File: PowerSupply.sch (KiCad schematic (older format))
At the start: 0 parts

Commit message: Arranged and annoted schematic
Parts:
- added C1, C2: CP, symbol Device:CP
- added D1, D2, D3, D4: 1N4007, Diode_THT:D_DO-41_SOD81_P10.16mm_Horizontal, symbol Diode:1N4007
- added D5, D6: LED, symbol Device:LED
- added J1: Barrel_Jack_Switch, symbol Connector:Barrel_Jack_Switch
- added J2, J3: Conn_02x02_Odd_Even, symbol Connector_Generic:Conn_02x02_Odd_Even
- added R1, R2: R, symbol Device:R
- added SW1: SW_DPDT_x2, symbol Switch:SW_DPDT_x2
- added U1: LM7805_TO220, Package_TO_SOT_THT:TO-220-3_Vertical, symbol Regulator_Linear:LM7805_TO220
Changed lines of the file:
@@
 Comment4 ""
 $EndDescr
+$Comp
+L Regulator_Linear:LM7805_TO220 U1
+U 1 1 5CD35ECB
+P 6625 3800
+F 0 "U1" H 6625 4042 50  0000 C CNN
+F 1 "LM7805_TO220" H 6625 3951 50  0000 C CNN
+F 2 "Package_TO_SOT_THT:TO-220-3_Vertical" H 6625 4025 50  0001 C CIN
+F 3 "http://www.fairchildsemi.com/ds/LM/LM7805.pdf" H 6625 3750 50  0001 C CNN
+	1    6625 3800
+	1    0    0    -1
+$EndComp
+$Comp
+L Diode:1N4007 D1
+U 1 1 5CD37B26
+P 4425 3950
+F 0 "D1" V 4379 4029 50  0000 L CNN
+F 1 "1N4007" V 4470 4029 50  0000 L CNN
+F 2 "Diode_THT:D_DO-41_SOD81_P10.16mm_Horizontal" H 4425 3775 50  0001 C CNN
+F 3 "http://www.vishay.com/docs/88503/1n4001.pdf" H 4425 3950 50  0001 C CNN
+	1    4425 3950
+	0    1    1    0
+$EndComp
+$Comp
+L Diode:1N4007 D3
+U 1 1 5CD3F3AA
+P 5075 3950
+F 0 "D3" V 5029 4029 50  0000 L CNN
+F 1 "1N4007" V 5120 4029 50  0000 L CNN
+F 2 "Diode_THT:D_DO-41_SOD81_P10.16mm_Horizontal" H 5075 3775 50  0001 C CNN
+F 3 "http://www.vishay.com/docs/88503/1n4001.pdf" H 5075 3950 50  0001 C CNN
+	1    5075 3950
+	0    1    1    0
+$EndComp
+$Comp
+L Diode:1N4007 D2
+U 1 1 5CD3FE81
+P 4425 4550
+F 0 "D2" V 4379 4629 50  0000 L CNN
+F 1 "1N4007" V 4470 4629 50  0000 L CNN
+F 2 "Diode_THT:D_DO-41_SOD81_P10.16mm_Horizontal" H 4425 4375 50  0001 C CNN
+F 3 "http://www.vishay.com/docs/88503/1n4001.pdf" H 4425 4550 50  0001 C CNN
+	1    4425 4550
+	0    1    1    0
+$EndComp
+$Comp
+L Diode:1N4007 D4
+U 1 1 5CD40742
+P 5075 4550
+F 0 "D4" V 5029 4629 50  0000 L CNN
+F 1 "1N4007" V 5120 4629 50  0000 L CNN
+F 2 "Diode_THT:D_DO-41_SOD81_P10.16mm_Horizontal" H 5075 4375 50  0001 C CNN
+F 3 "http://www.vishay.com/docs/88503/1n4001.pdf" H 5075 4550 50  0001 C CNN
+	1    5075 4550
+	0    1    1    0
+$EndComp
+$Comp
+L Device:CP C1
+U 1 1 5CD41669
+P 5825 3925
+F 0 "C1" H 5943 3971 50  0000 L CNN
+F 1 "CP" H 5943 3880 50  0000 L CNN
+F 2 "" H 5863 3775 50  0001 C CNN
+F 3 "~" H 5825 3925 50  0001 C CNN
+	1    5825 3925
+	1    0    0    -1
+$EndComp
+$Comp
+L Device:CP C2
+U 1 1 5CD42457
+P 7300 3925
+F 0 "C2" H 7418 3971 50  0000 L CNN
+F 1 "CP" H 7418 3880 50  0000 L CNN
+F 2 "" H 7338 3775 50  0001 C CNN
+F 3 "~" H 7300 3925 50  0001 C CNN
+	1    7300 3925
+	1    0    0    -1
+$EndComp
+$Comp
+L Device:LED D6
+U 1 1 5CD42B2D
+P 8925 4400
+F 0 "D6" V 8964 4283 50  0000 R CNN
+F 1 "LED" V 8873 4283 50  0000 R CNN
+F 2 "" H 8925 4400 50  0001 C CNN
+F 3 "~" H 8925 4400 50  0001 C CNN
+	1    8925 4400
+	0    -1   -1   0
+$EndComp
+$Comp
+L Device:LED D5
+U 1 1 5CD441AD
+P 7825 4400
+F 0 "D5" V 7864 4283 50  0000 R CNN
+F 1 "LED" V 7773 4283 50  0000 R CNN
+F 2 "" H 7825 4400 50  0001 C CNN
+F 3 "~" H 7825 4400 50  0001 C CNN
+	1    7825 4400
+	0    -1   -1   0
+$EndComp
+$Comp
+L Device:R R1
+U 1 1 5CD44A91
+P 7825 3900
+F 0 "R1" H 7755 3854 50  0000 R CNN
+F 1 "R" H 7755 3945 50  0000 R CNN
+F 2 "" V 7755 3900 50  0001 C CNN
+F 3 "~" H 7825 3900 50  0001 C CNN
+	1    7825 3900
+	-1   0    0    1
+$EndComp
+$Comp
+L Device:R R2
+U 1 1 5CD45C68
+P 8925 3900
+F 0 "R2" H 8855 3854 50  0000 R CNN
+F 1 "R" H 8855 3945 50  0000 R CNN
+F 2 "" V 8855 3900 50  0001 C CNN
+F 3 "~" H 8925 3900 50  0001 C CNN
+	1    8925 3900
+	-1   0    0    1
+$EndComp
+$Comp
+L Switch:SW_DPDT_x2 SW1
+U 1 1 5CD465F3
+P 8425 4175
+F 0 "SW1" H 8425 4460 50  0000 C CNN
+F 1 "SW_DPDT_x2" H 8425 4369 50  0000 C CNN
+F 2 "" H 8425 4175 50  0001 C CNN
+F 3 "~" H 8425 4175 50  0001 C CNN
+	1    8425 4175
+	1    0    0    -1
+$EndComp
+$Comp
+L Connector_Generic:Conn_02x02_Odd_Even J2
+U 1 1 5CD47BF0
+P 9800 3925
+F 0 "J2" H 9850 4142 50  0000 C CNN
+F 1 "Conn_02x02_Odd_Even" H 9850 4051 50  0000 C CNN
+F 2 "" H 9800 3925 50  0001 C CNN
+F 3 "~" H 9800 3925 50  0001 C CNN
+	1    9800 3925
+	1    0    0    -1
+$EndComp
+$Comp
+L Connector_Generic:Conn_02x02_Odd_Even J3
+U 1 1 5CD48B93
+P 9800 4475
+F 0 "J3" H 9850 4692 50  0000 C CNN
+F 1 "Conn_02x02_Odd_Even" H 9850 4601 50  0000 C CNN
+F 2 "" H 9800 4475 50  0001 C CNN
+F 3 "~" H 9800 4475 50  0001 C CNN
+	1    9800 4475
+	1    0    0    -1
+$EndComp
+$Comp
+L Connector:Barrel_Jack_Switch J1
+U 1 1 5CD495E1
+P 3825 4325
+F 0 "J1" H 3882 4642 50  0000 C CNN
+F 1 "Barrel_Jack_Switch" H 3882 4551 50  0000 C CNN
+F 2 "" H 3875 4285 50  0001 C CNN
+F 3 "~" H 3875 4285 50  0001 C CNN
+	1    3825 4325
+	1    0    0    -1
+$EndComp
 $EndSCHEMATC

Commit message: Added footprint associations to schematic components
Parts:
- C1: footprint (none) -> Capacitor_THT:CP_Radial_D10.0mm_P5.00mm
- C2: footprint (none) -> Capacitor_THT:CP_Radial_D6.3mm_P2.50mm
- D5, D6: footprint (none) -> LED_THT:LED_D5.0mm
- J1: footprint (none) -> Connector_BarrelJack:BarrelJack_CUI_PJ-102AH_Horizontal
- J2, J3: footprint (none) -> Connector_PinHeader_2.54mm:PinHeader_2x02_P2.54mm_Vertical
- R1, R2: footprint (none) -> Resistor_THT:R_Axial_DIN0207_L6.3mm_D2.5mm_P7.62mm_Horizontal
- SW1: footprint (none) -> digikey-footprints:Switch_Slide_11.6x4mm_EG1218
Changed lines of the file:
@@
 F 0 "C1" H 5943 3971 50  0000 L CNN
 F 1 "CP" H 5943 3880 50  0000 L CNN
-F 2 "" H 5863 3775 50  0001 C CNN
+F 2 "Capacitor_THT:CP_Radial_D10.0mm_P5.00mm" H 5863 3775 50  0001 C CNN
 F 3 "~" H 5825 3925 50  0001 C CNN
 	1    5825 3925
@@
 F 0 "C2" H 7418 3971 50  0000 L CNN
 F 1 "CP" H 7418 3880 50  0000 L CNN
-F 2 "" H 7338 3775 50  0001 C CNN
+F 2 "Capacitor_THT:CP_Radial_D6.3mm_P2.50mm" H 7338 3775 50  0001 C CNN
 F 3 "~" H 7300 3925 50  0001 C CNN
 	1    7300 3925
@@
 F 0 "D6" V 8964 4283 50  0000 R CNN
 F 1 "LED" V 8873 4283 50  0000 R CNN
-F 2 "" H 8925 4400 50  0001 C CNN
+F 2 "LED_THT:LED_D5.0mm" H 8925 4400 50  0001 C CNN
 F 3 "~" H 8925 4400 50  0001 C CNN
 	1    8925 4400
@@
 F 0 "D5" V 7864 4283 50  0000 R CNN
 F 1 "LED" V 7773 4283 50  0000 R CNN
-F 2 "" H 7825 4400 50  0001 C CNN
+F 2 "LED_THT:LED_D5.0mm" H 7825 4400 50  0001 C CNN
 F 3 "~" H 7825 4400 50  0001 C CNN
 	1    7825 4400
@@
 F 0 "R1" H 7755 3854 50  0000 R CNN
 F 1 "R" H 7755 3945 50  0000 R CNN
-F 2 "" V 7755 3900 50  0001 C CNN
+F 2 "Resistor_THT:R_Axial_DIN0207_L6.3mm_D2.5mm_P7.62mm_Horizontal" V 7755 3900 50  0001 C CNN
 F 3 "~" H 7825 3900 50  0001 C CNN
 	1    7825 3900
@@
 F 0 "R2" H 8855 3854 50  0000 R CNN
 F 1 "R" H 8855 3945 50  0000 R CNN
-F 2 "" V 8855 3900 50  0001 C CNN
+F 2 "Resistor_THT:R_Axial_DIN0207_L6.3mm_D2.5mm_P7.62mm_Horizontal" V 8855 3900 50  0001 C CNN
 F 3 "~" H 8925 3900 50  0001 C CNN
 	1    8925 3900
@@
 F 0 "SW1" H 8425 4460 50  0000 C CNN
 F 1 "SW_DPDT_x2" H 8425 4369 50  0000 C CNN
-F 2 "" H 8425 4175 50  0001 C CNN
+F 2 "digikey-footprints:Switch_Slide_11.6x4mm_EG1218" H 8425 4175 50  0001 C CNN
 F 3 "~" H 8425 4175 50  0001 C CNN
 	1    8425 4175
@@
 F 0 "J2" H 9850 4142 50  0000 C CNN
 F 1 "Conn_02x02_Odd_Even" H 9850 4051 50  0000 C CNN
-F 2 "" H 9800 3925 50  0001 C CNN
+F 2 "Connector_PinHeader_2.54mm:PinHeader_2x02_P2.54mm_Vertical" H 9800 3925 50  0001 C CNN
 F 3 "~" H 9800 3925 50  0001 C CNN
 	1    9800 3925
@@
 F 0 "J3" H 9850 4692 50  0000 C CNN
 F 1 "Conn_02x02_Odd_Even" H 9850 4601 50  0000 C CNN
-F 2 "" H 9800 4475 50  0001 C CNN
+F 2 "Connector_PinHeader_2.54mm:PinHeader_2x02_P2.54mm_Vertical" H 9800 4475 50  0001 C CNN
 F 3 "~" H 9800 4475 50  0001 C CNN
 	1    9800 4475
@@
 F 0 "J1" H 3882 4642 50  0000 C CNN
 F 1 "Barrel_Jack_Switch" H 3882 4551 50  0000 C CNN
-F 2 "" H 3875 4285 50  0001 C CNN
+F 2 "Connector_BarrelJack:BarrelJack_CUI_PJ-102AH_Horizontal" H 3875 4285 50  0001 C CNN
 F 3 "~" H 3875 4285 50  0001 C CNN
 	1    3825 4325

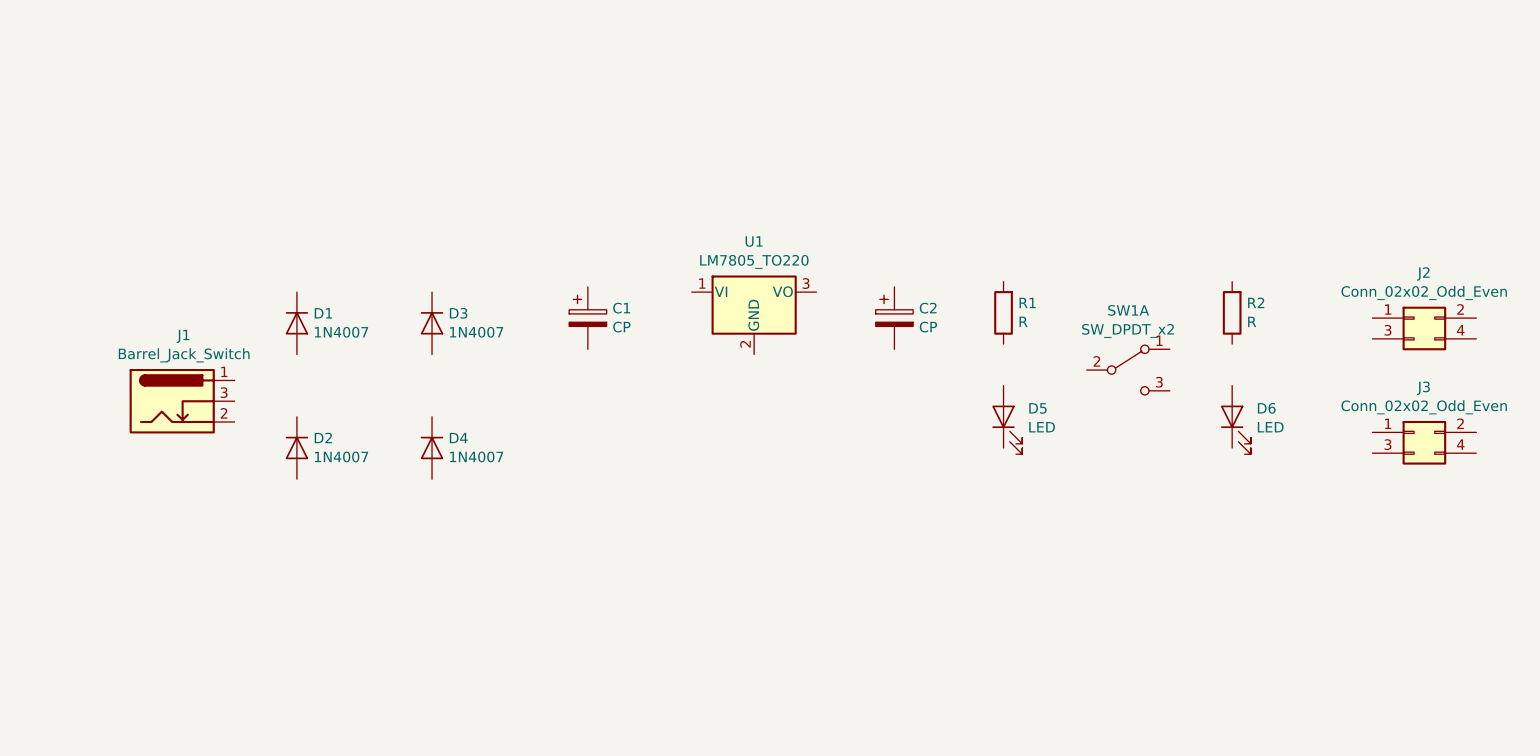
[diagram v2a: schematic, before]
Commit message: Completed the wiring of the schematic
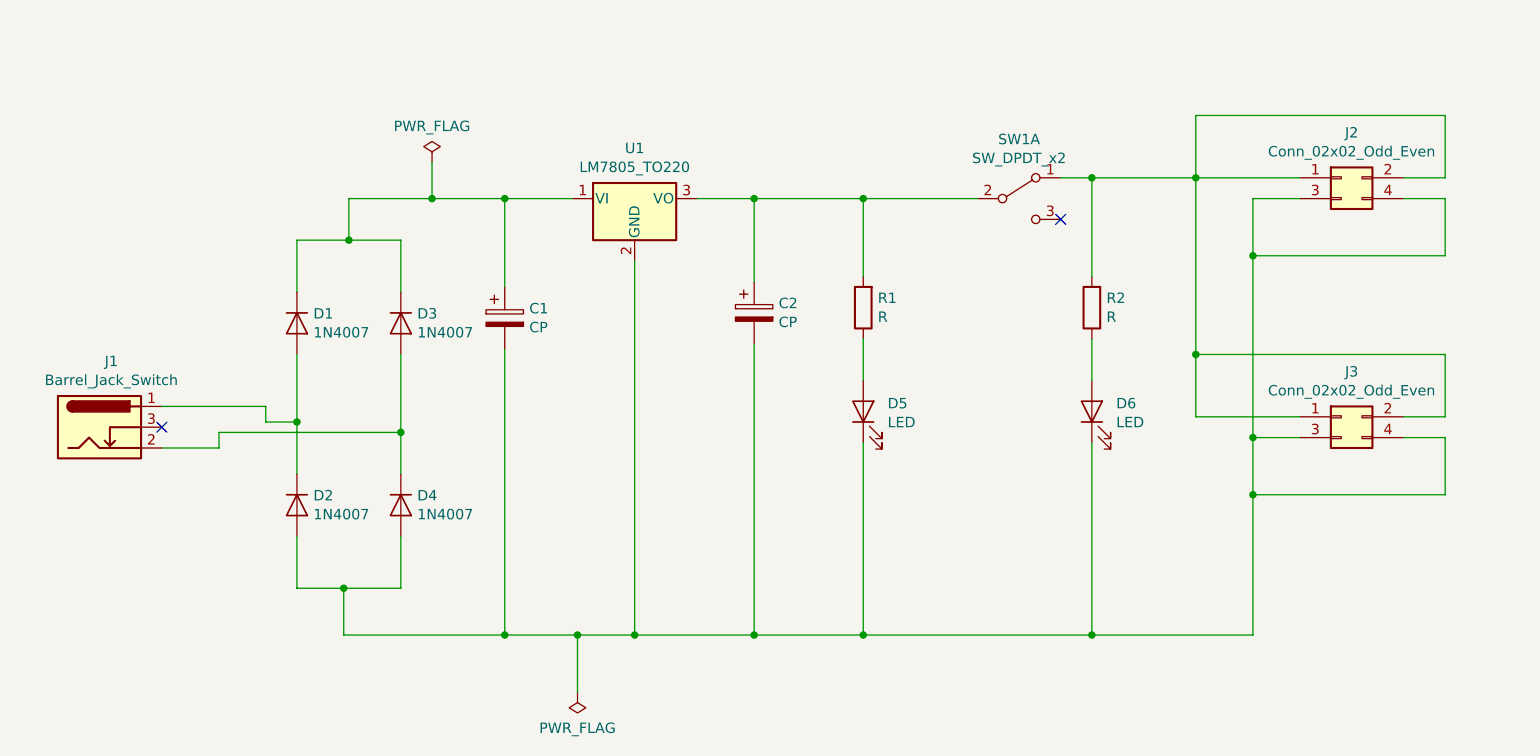
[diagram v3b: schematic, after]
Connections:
- net at U1.1 (VI): now also C1.1, D1.1 (K), D3.1 (K)
- net at U1.2 (GND): now also C1.2, C2.2, D2.2 (A), D4.2 (A), D5.1 (K), D6.1 (K), J2.3 (Pin_3), J2.4 (Pin_4), J3.3 (Pin_3), J3.4 (Pin_4)
- net at U1.3 (VO): now also C2.1, R1.2, SW1.2 (B)
- net at D1.2 (A): now also D2.1 (K), J1.1
- net at D3.2 (A): now also D4.1 (K), J1.2
- net at D6.2 (A): now also R2.1
- net at D5.2 (A): now also R1.1
- net at R2.2: now also J2.1 (Pin_1), J2.2 (Pin_2), J3.1 (Pin_1), J3.2 (Pin_2), SW1.1 (A)
- no-connect marks 0 -> 2
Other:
- moved on the sheet: C1, C2, D2, D3, D4, D5, D6, J1, J2, J3, R1, R2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

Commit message: Added Nets to schematic
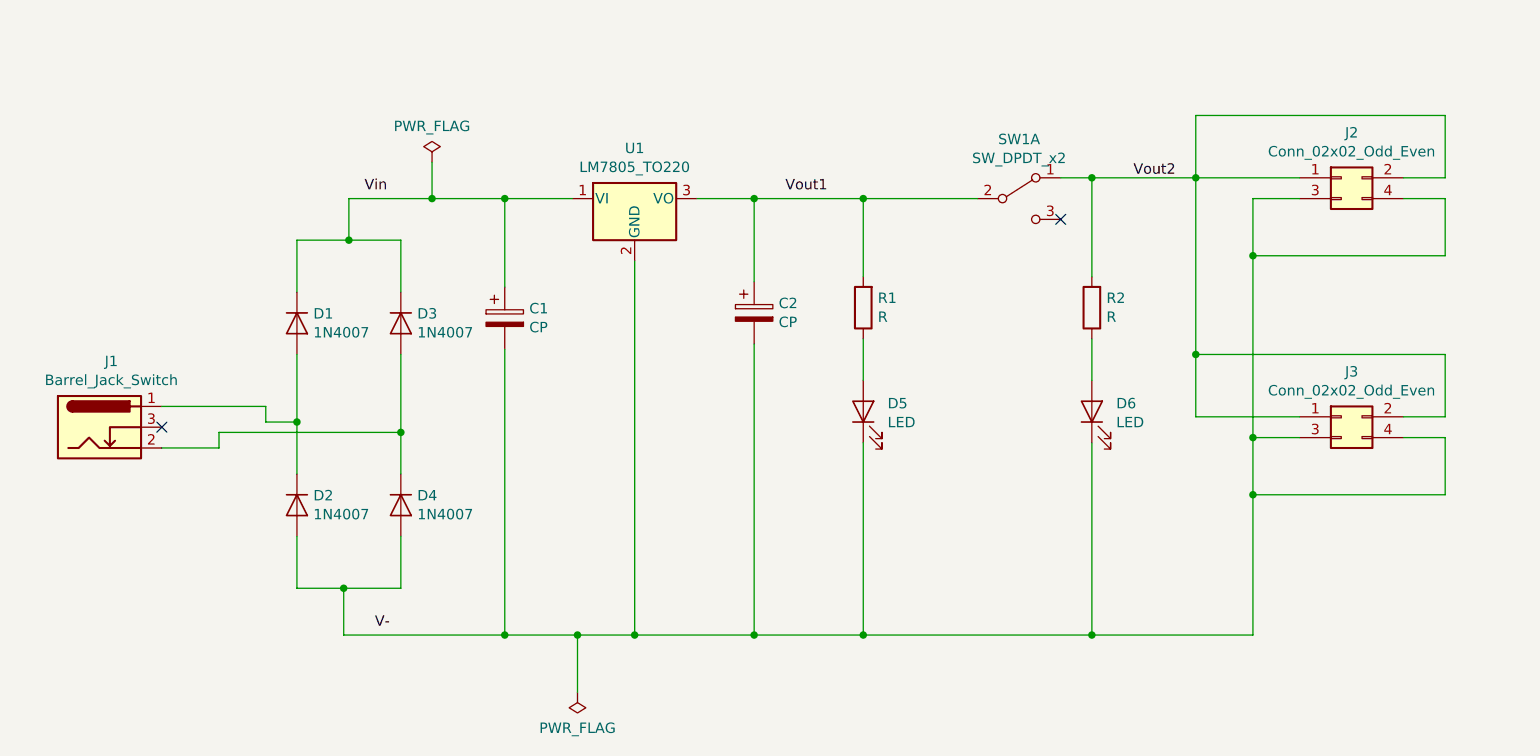
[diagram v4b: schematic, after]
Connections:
- net Vout2: now reaches J2.1 (Pin_1), J2.2 (Pin_2), J3.1 (Pin_1), J3.2 (Pin_2), R2.2, SW1.1 (A)
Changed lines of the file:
@@
 Wire Wire Line
 	5775 5450 6050 5450
+Text Label 4750 3325 0    50   ~ 0
+Vin
+Text Label 4800 5425 0    50   ~ 0
+V-
+Text Label 6775 3325 0    50   ~ 0
+Vout1
+Text Label 8450 3250 0    50   ~ 0
+Vout2
 $EndSCHEMATC

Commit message: Added comment notes
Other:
- note added: "N1 - Power Input"
- note added: "N2 - Bridge Rectifier"
- note added: "N3 - Voltage Regulator"
- note added: "N4 -\nPower\nIndicator"
- note added: "N5 - \nOn/Off Switch"
- note added: "N6 - \nOutput\nPWR Indicator"
- note added: "N7 - Power Output"
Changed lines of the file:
@@
 Text Label 8450 3250 0    50   ~ 0
 Vout2
+Wire Notes Line
+	4025 2750 4025 5750
+Wire Notes Line
+	4025 5750 3075 5750
+Wire Notes Line
+	3075 5750 3075 2750
+Wire Notes Line
+	3075 2750 4025 2750
+Wire Notes Line
+	4225 2750 4225 5750
+Wire Notes Line
+	4225 5750 5250 5750
+Wire Notes Line
+	5250 5750 5250 2750
+Wire Notes Line
+	5250 2750 4225 2750
+Wire Notes Line
+	5325 2750 5325 5750
+Wire Notes Line
+	5325 5750 7000 5750
+Wire Notes Line
+	7000 5750 7000 2750
+Wire Notes Line
+	7000 2750 5325 2750
+Wire Notes Line
+	7075 2750 7075 5725
+Wire Notes Line
+	7075 5725 7500 5725
+Wire Notes Line
+	7500 5725 7500 2750
+Wire Notes Line
+	7500 2750 7075 2750
+Wire Notes Line
+	7575 2750 7575 5750
+Wire Notes Line
+	7575 5750 8150 5750
+Wire Notes Line
+	8150 5750 8150 2750
+Wire Notes Line
+	8150 2750 7575 2750
+Wire Notes Line
+	8175 5750 8675 5750
+Wire Notes Line
+	8675 5750 8675 2750
+Wire Notes Line
+	8675 2750 8175 2750
+Wire Notes Line
+	8175 2750 8175 5750
+Wire Notes Line
+	8725 2675 8725 5750
+Wire Notes Line
+	8725 5750 10075 5750
+Wire Notes Line
+	10075 5750 10075 2675
+Wire Notes Line
+	10075 2675 8725 2675
+Text Notes 3075 2725 0    50   ~ 0
+N1 - Power Input
+Text Notes 4225 2725 0    50   ~ 0
+N2 - Bridge Rectifier
+Text Notes 5325 2725 0    50   ~ 0
+N3 - Voltage Regulator
+Text Notes 7075 2725 0    50   ~ 0
+N4 -\nPower\nIndicator
+Text Notes 7575 2725 0    50   ~ 0
+N5 - \nOn/Off Switch
+Text Notes 8150 2725 0    50   ~ 0
+N6 - \nOutput\nPWR Indicator
+Text Notes 8725 2625 0    50   ~ 0
+N7 - Power Output
 $EndSCHEMATC
